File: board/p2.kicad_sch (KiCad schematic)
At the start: 6 parts, among them SW1 SW_Push, U1 ESP32-DevKitC

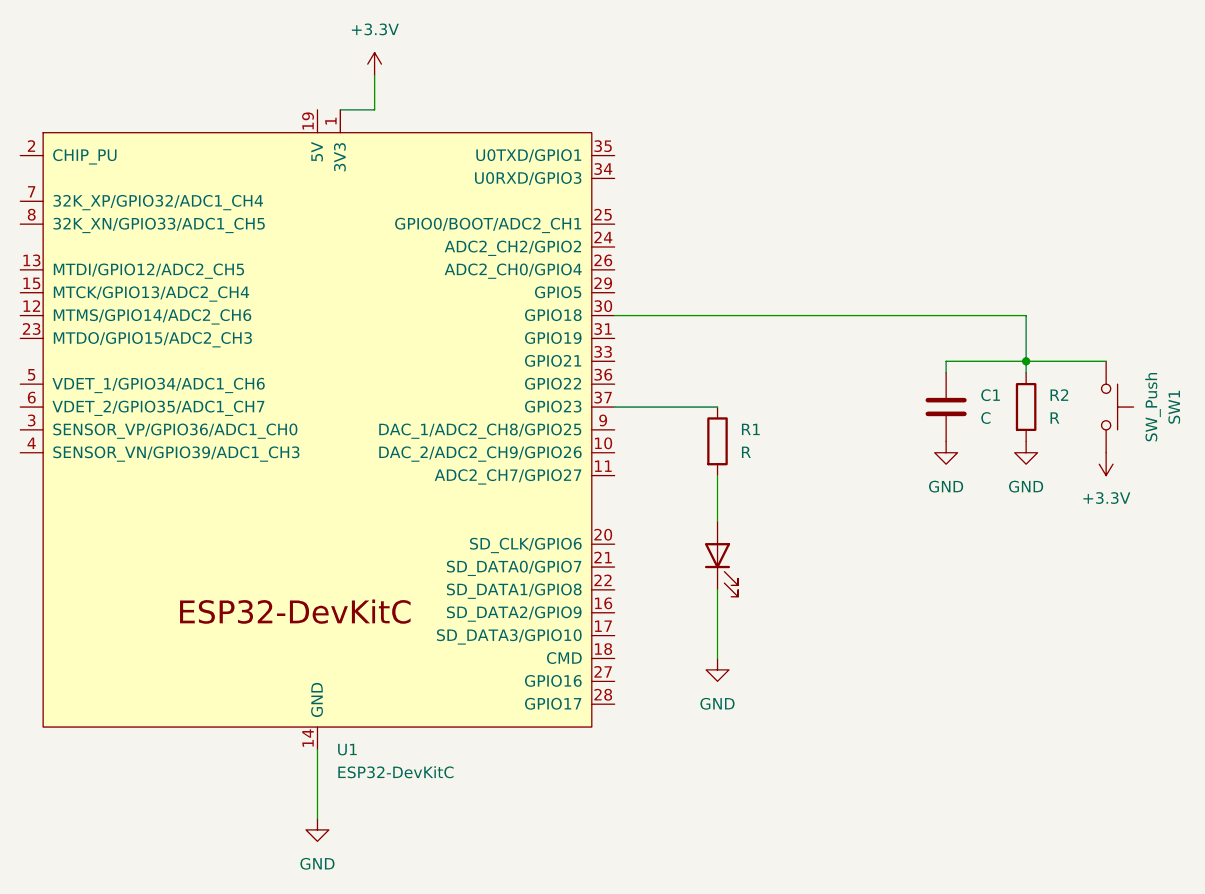
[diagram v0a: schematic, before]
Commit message: fix(gpio): solve state desync by reading hardware in ISR
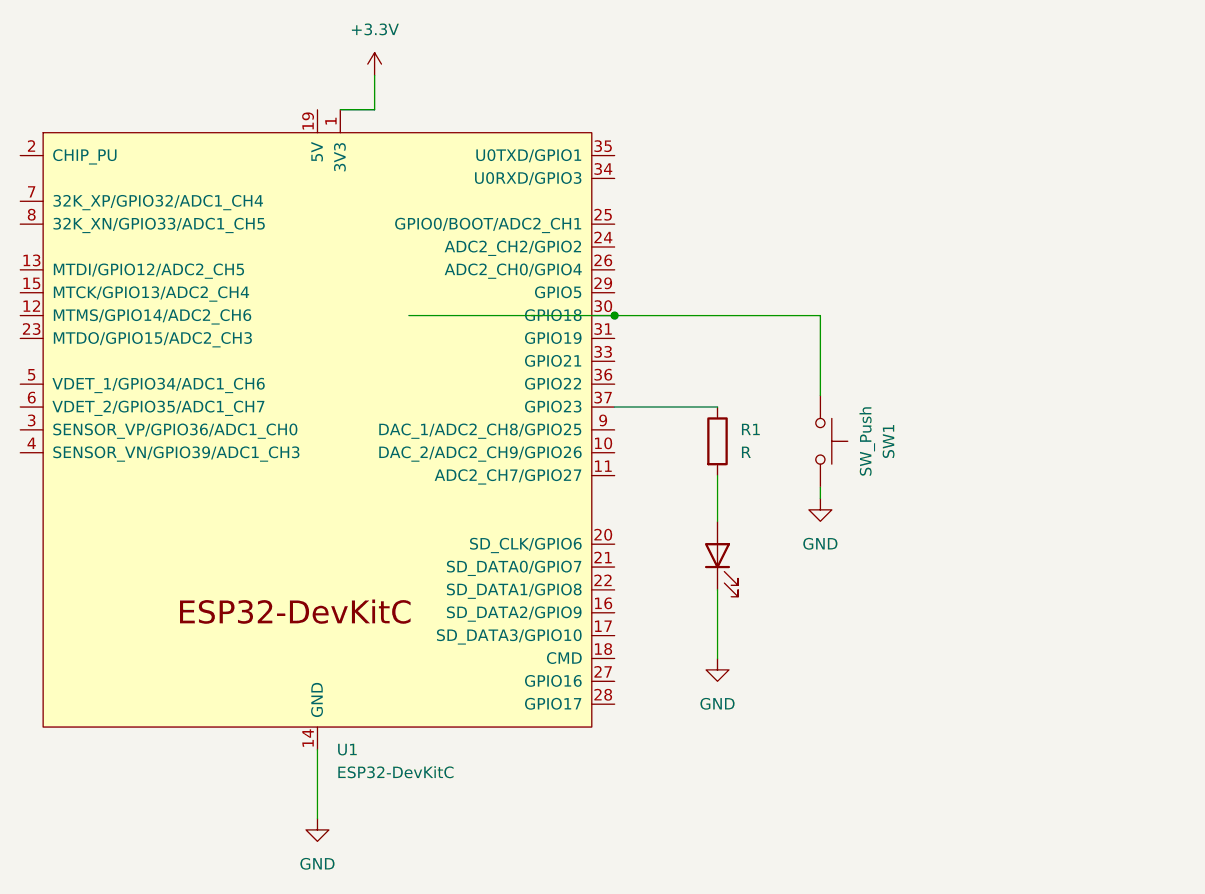
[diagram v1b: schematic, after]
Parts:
- removed C1: C, Capacitor_THT:C_Disc_D5.0mm_W2.5mm_P5.00mm, symbol Device:C
- removed R2: R, Resistor_THT:R_Axial_DIN0207_L6.3mm_D2.5mm_P7.62mm_Horizontal, symbol Device:R
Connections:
- net +3.3V: no longer SW1.2
- net GND: now also SW1.2
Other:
- moved on the sheet: SW1
